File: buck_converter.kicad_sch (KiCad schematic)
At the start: 46 parts, among them U3 LMR604403SRAKR, U4 LMR604403SRAKR

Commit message: update sch
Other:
- title: RSC hat board -> RSC hat board - TorxHAT
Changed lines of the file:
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@@
 	(paper "A4")
 	(title_block
-		(title "RSC hat board")
-		(date "2026-06-01")
-		(rev "A")
-		(comment 1 "Author: Raiko Torga")
+		(title "RSC hat board - TorxHAT")
+		(date "2026-07-17")
+		(rev "B")
+		(comment 1 "Authors: Raiko Torga, Matevz B. Zorec")
 	)
 	(text "Input: DC 9 V - 20 V Output: 5.1 V at 4 A each\nhttps://www.ti.com/lit/ds/symlink/lmr60440.pdf"

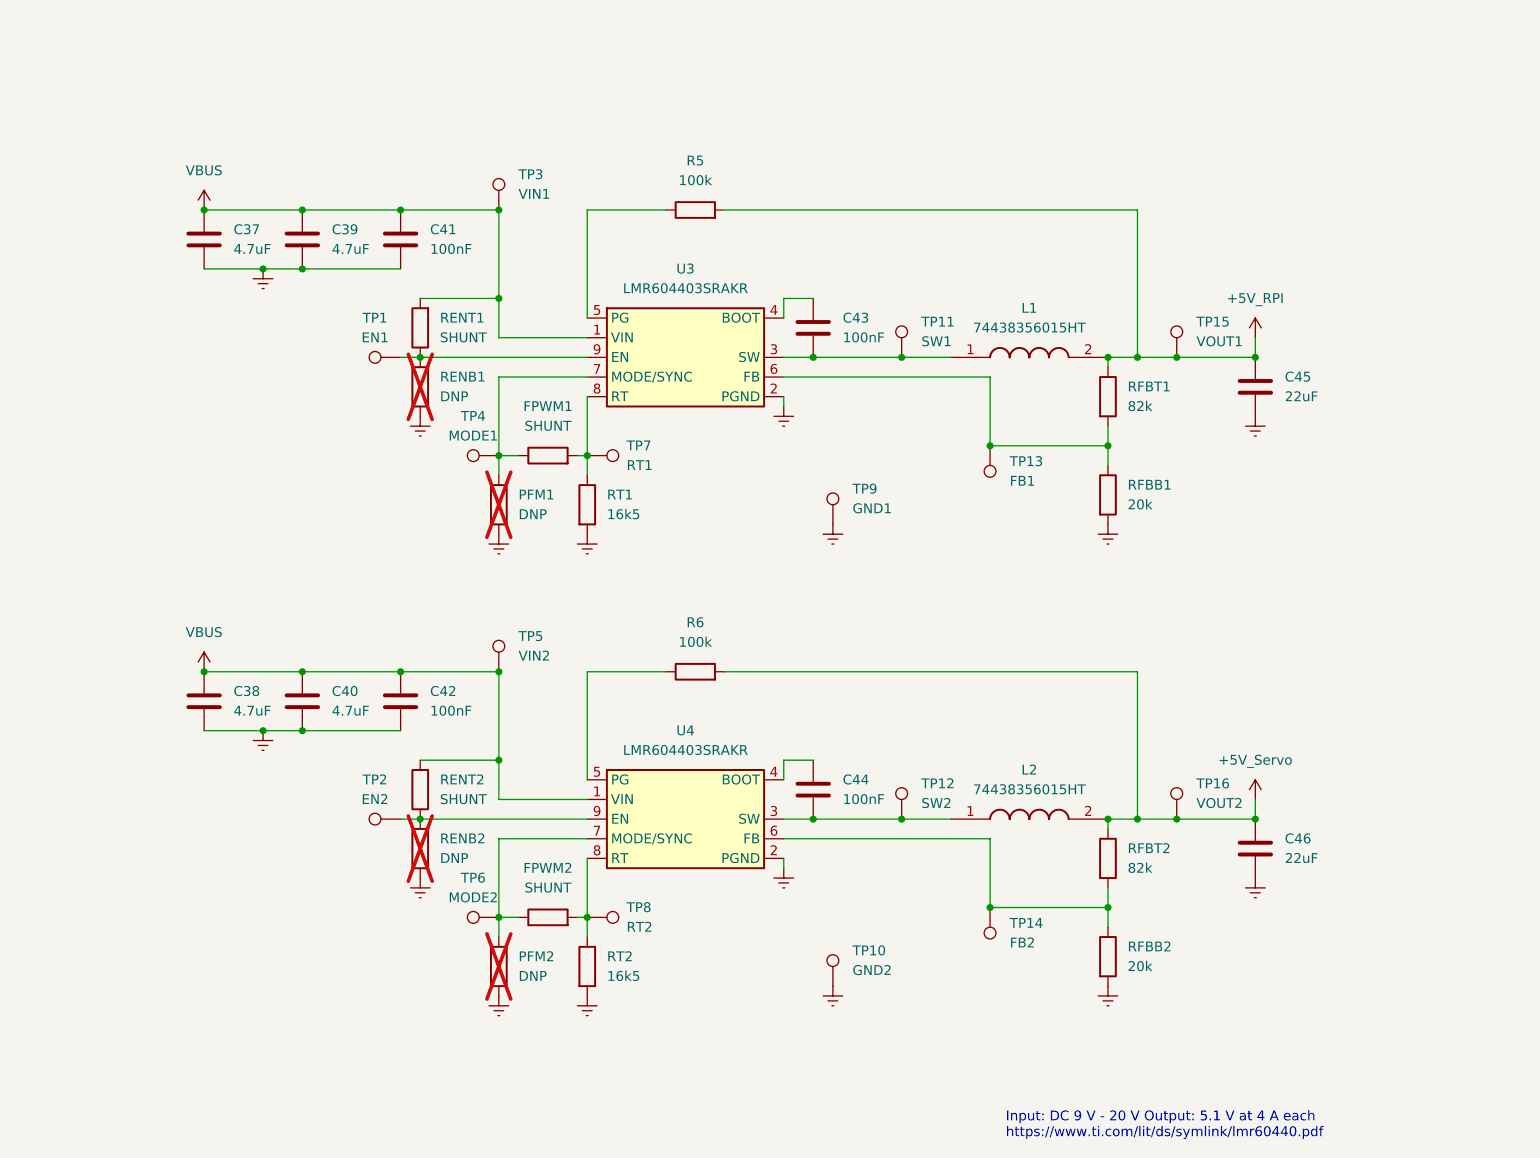
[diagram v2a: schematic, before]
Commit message: update; add EN servo rail ctrl via GPIO05
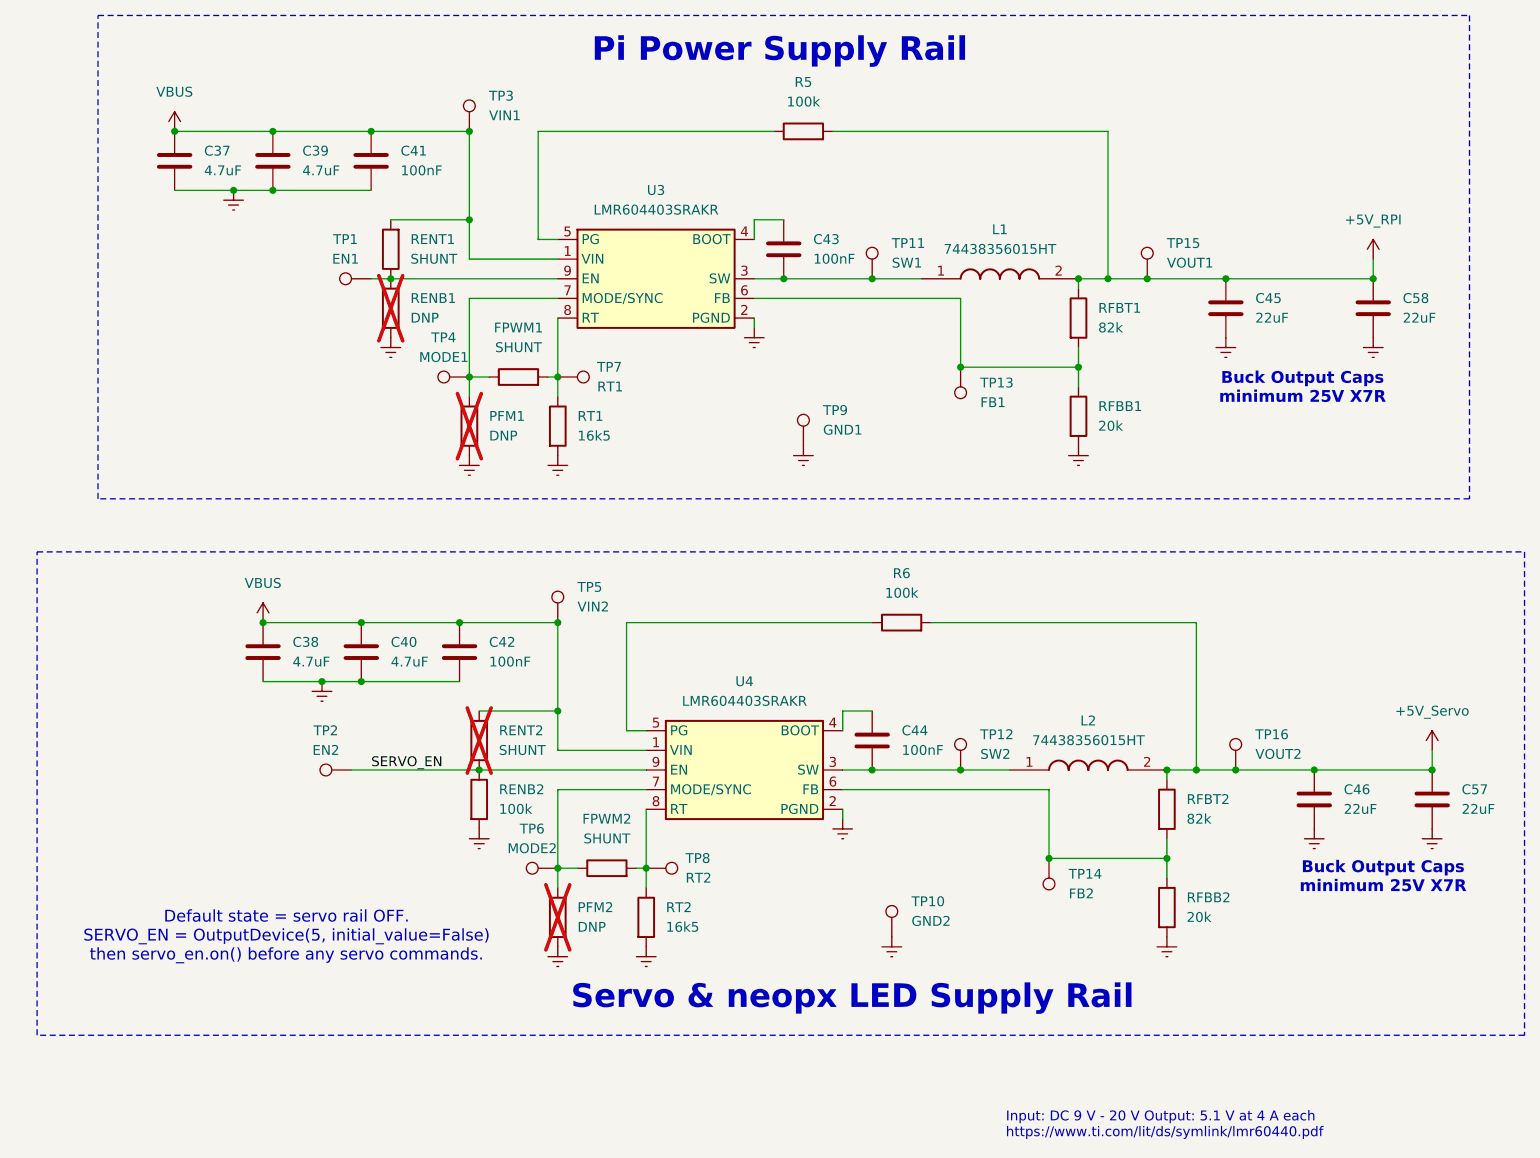
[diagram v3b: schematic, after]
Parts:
- added C57, C58: 22uF, Capacitor_SMD:C_0805_2012Metric_Pad1.18x1.45mm_HandSolder, symbol Device:C
- RENB2: value DNP -> 100k; now fitted
- RENT2: now not fitted
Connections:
- net +5V_RPI: now also C58.1
- net +5V_Servo: now also C57.1
- net GND: now also C57.2, C58.2
- net SERVO_EN: now reaches RENB2.1, RENT2.1, TP2.1, U4.9 (EN)
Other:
- note added: "Buck Output Caps minimum 25V X7R"
- note added: "Default state = servo rail OFF. SERVO_EN = OutputDevice(5, initial_value=False) then servo_en.on() before any servo commands."
- note added: "Pi Power Supply Rail"
- note added: "Servo & neopx LED Supply Rail"
- moved on the sheet: C37, C38, C39, C40, C41, C42, C43, C44, C45, C46, FPWM1, FPWM2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

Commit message: progress alhamdulliah... last batch = buck stage patches + thermal via spam
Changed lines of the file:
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@@
 	)
 	(junction
+		(at 217.17 59.69)
+		(diameter 0)
+		(color 0 0 0 0)
+	)
+	(junction
 		(at 203.2 123.19)
 		(diameter 0)
@@
 	)
 	(junction
+		(at 224.79 123.19)
+		(diameter 0)
+		(color 0 0 0 0)
+	)
+	(junction
 		(at 208.28 123.19)
 		(diameter 0)
@@
 	(wire
 		(pts
-			(xy 226.06 59.69) (xy 207.01 59.69)
+			(xy 226.06 59.69) (xy 217.17 59.69)
 		)
 		(stroke
@@
 	(wire
 		(pts
+			(xy 224.79 123.19) (xy 233.68 123.19)
+		)
+		(stroke
+			(width 0)
+			(type default)
+		)
+	)
+	(wire
+		(pts
 			(xy 132.08 135.89) (xy 132.08 138.43)
 		)
@@
 	(wire
 		(pts
-			(xy 218.44 123.19) (xy 233.68 123.19)
+			(xy 218.44 123.19) (xy 224.79 123.19)
 		)
 		(stroke
@@
 	(wire
 		(pts
+			(xy 217.17 59.69) (xy 207.01 59.69)
+		)
+		(stroke
+			(width 0)
+			(type default)
+		)
+	)
+	(wire
+		(pts
 			(xy 93.98 123.19) (xy 132.08 123.19)
 		)
@@
 	)
 	(symbol
+		(lib_id "power:PWR_FLAG")
+		(at 224.79 123.19 0)
+		(unit 1)
+		(body_style 1)
+		(exclude_from_sim no)
+		(in_bom yes)
+		(on_board yes)
+		(in_pos_files yes)
+		(dnp no)
+		(fields_autoplaced yes)
+		(property "Reference" "#FLG03"
+			(at 224.79 121.285 0)
+			(hide yes)
+			(show_name no)
+			(do_not_autoplace no)
+			(effects
+				(font
+					(size 1.27 1.27)
+				)
+			)
+		)
+		(property "Value" "PWR_FLAG"
+			(at 224.79 118.11 0)
+			(show_name no)
+			(do_not_autoplace no)
+			(effects
+				(font
+					(size 1.27 1.27)
+				)
+			)
+		)
+		(property "Footprint" ""
+			(at 224.79 123.19 0)
+			(hide yes)
+			(show_name no)
+			(do_not_autoplace no)
+			(effects
+				(font
+					(size 1.27 1.27)
+				)
+			)
+		)
+		(property "Datasheet" ""
+			(at 224.79 123.19 0)
+			(hide yes)
+			(show_name no)
+			(do_not_autoplace no)
+			(effects
+				(font
+					(size 1.27 1.27)
+				)
+			)
+		)
+		(property "Description" "Special symbol for telling ERC where power comes from"
+			(at 224.79 123.19 0)
+			(hide yes)
+			(show_name no)
+			(do_not_autoplace no)
+			(effects
+				(font
+					(size 1.27 1.27)
+				)
+			)
+		)
+		(pin "1"
+		)
+		(instances
+			(project "RSC_extension_board"
+				(path "/1f48ed4c-84ce-4e77-88fc-25bf92dcee2d/8a23fee1-8a0a-4a00-88d2-3a4147ed7fcf"
+					(reference "#FLG03")
+					(unit 1)
+				)
+			)
+		)
+	)
+	(symbol
 		(lib_id "Device:R")
 		(at 187.96 64.77 0)
@@
 					(unit 1)
 				)
+			)
+		)
+	)
+	(symbol
+		(lib_id "power:PWR_FLAG")
+		(at 217.17 59.69 0)
+		(unit 1)
+		(body_style 1)
+		(exclude_from_sim no)
+		(in_bom yes)
+		(on_board yes)
+		(in_pos_files yes)
+		(dnp no)
+		(fields_autoplaced yes)
+		(property "Reference" "#FLG04"
+			(at 217.17 57.785 0)
+			(hide yes)
+			(show_name no)
+			(do_not_autoplace no)
+			(effects
+				(font
+					(size 1.27 1.27)
+				)
+			)
+		)
+		(property "Value" "PWR_FLAG"
+			(at 217.17 54.61 0)
+			(show_name no)
+			(do_not_autoplace no)
+			(effects
+				(font
+					(size 1.27 1.27)
+				)
+			)
+		)
+		(property "Footprint" ""
+			(at 217.17 59.69 0)
+			(hide yes)
+			(show_name no)
+			(do_not_autoplace no)
+			(effects
+				(font
+					(size 1.27 1.27)
+				)
+			)
+		)
+		(property "Datasheet" ""
+			(at 217.17 59.69 0)
+			(hide yes)
+			(show_name no)
+			(do_not_autoplace no)
+			(effects
+				(font
+					(size 1.27 1.27)
+				)
+			)
+		)
+		(property "Description" "Special symbol for telling ERC where power comes from"
+			(at 217.17 59.69 0)
+			(hide yes)
+			(show_name no)
+			(do_not_autoplace no)
+			(effects
+				(font
+					(size 1.27 1.27)
+				)
+			)
+		)
+		(pin "1"
+		)
+		(instances
+			(project "RSC_extension_board"
+				(path "/1f48ed4c-84ce-4e77-88fc-25bf92dcee2d/8a23fee1-8a0a-4a00-88d2-3a4147ed7fcf"
+					(reference "#FLG04")
+					(unit 1)
+				)

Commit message: preliminary layout complete, DRC passed; consolidating BOM - may have to switch top header (hence new footprint potentially!)
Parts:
- removed TP10: GND2, TestPoint:TestPoint_Pad_D1.0mm, symbol Connector:TestPoint
- removed TP9: GND1, TestPoint:TestPoint_Pad_D1.0mm, symbol Connector:TestPoint
